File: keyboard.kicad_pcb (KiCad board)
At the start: 2 copper layers, 355 x 150.1 mm, 145 parts, among them SW1 SW_Push, SW10 SW_Push, SW11 SW_Push, SW12 SW_Push, SW13 SW_Push, SW14 SW_Push, SW15 SW_Push, SW16 SW_Push, SW17 SW_Push, SW18 SW_Push, SW19 SW_Push, SW2 SW_Push, SW20 SW_Push, SW21 SW_Push, SW22 SW_Push, SW23 SW_Push, SW24 SW_Push, SW25 SW_Push, SW26 SW_Push, SW27 SW_Push, SW28 SW_Push, SW29 SW_Push, SW3 SW_Push, SW30 SW_Push, SW31 SW_Push, SW32 SW_Push, SW33 SW_Push, SW34 SW_Push, SW35 SW_Push, SW36 SW_Push, SW37 SW_Push, SW38 SW_Push, SW39 SW_Push, SW4 SW_Push, SW40 SW_Push, SW41 SW_Push, SW42 SW_Push, SW43 SW_Push, SW44 SW_Push, SW45 SW_Push, SW46 SW_Push, SW47 SW_Push, SW48 SW_Push, SW49 SW_Push, SW5 SW_Push, SW50 SW_Push, SW51 SW_Push, SW52 SW_Push, SW53 SW_Push, SW54 SW_Push, SW55 SW_Push, SW56 SW_Push, SW57 SW_Push, SW58 SW_Push, SW59 SW_Push, SW6 SW_Push, SW60 SW_Push, SW61 SW_Push, SW62 SW_Push, SW63 SW_Push, SW64 SW_Push, SW7 SW_Push, SW8 SW_Push, SW9 SW_Push, U1 Pro Micro, U2 TRRS, U3 Pro Micro, U4 TRRS

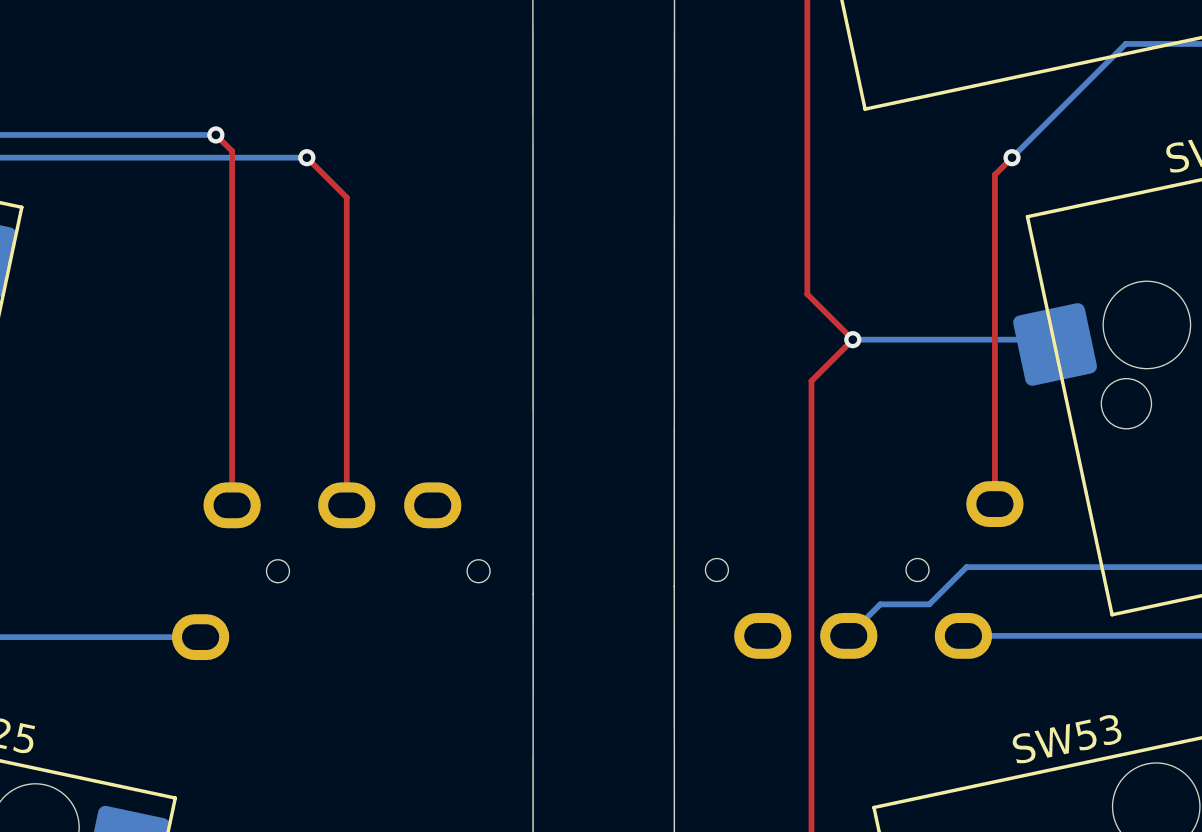
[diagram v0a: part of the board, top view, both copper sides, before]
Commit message: Move TRRS jacks around
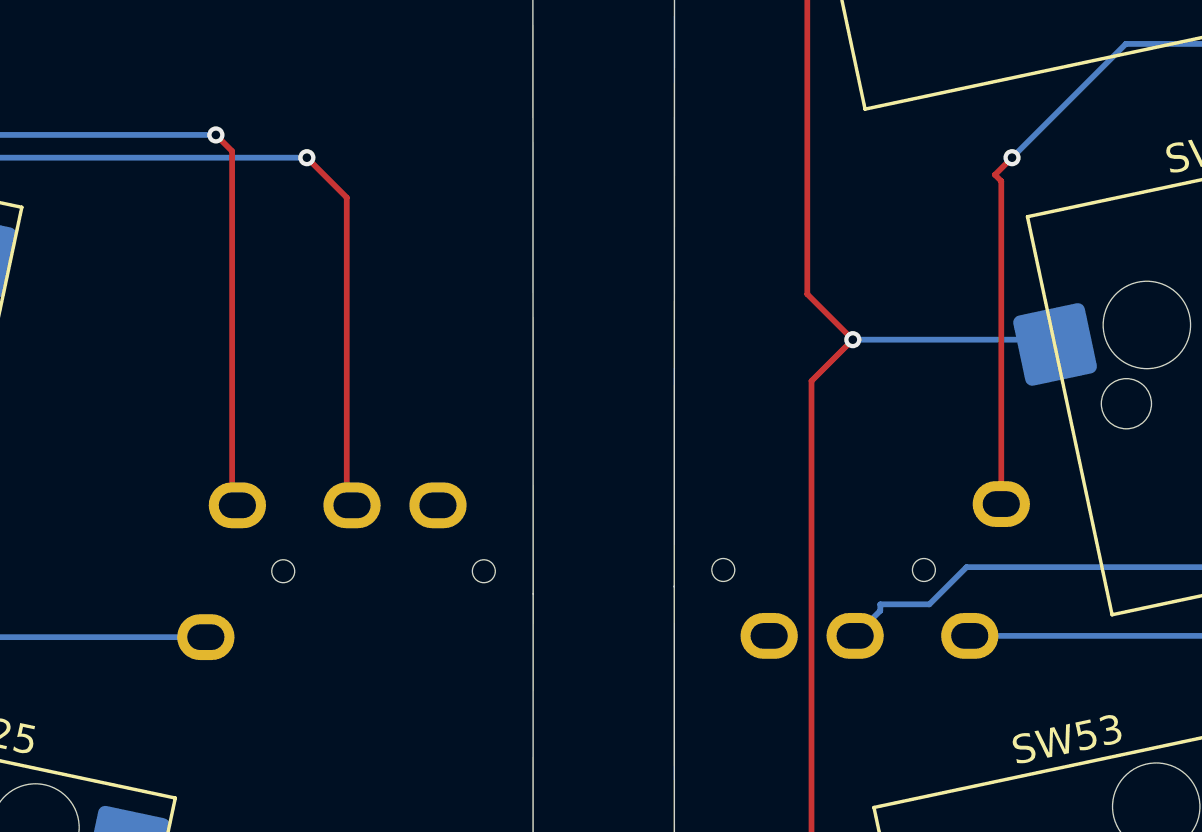
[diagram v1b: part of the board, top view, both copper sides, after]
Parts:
- moved U4 0.22 mm to (207.4, 152.5)
- moved U2 0.18 mm to (202.2, 152.5)
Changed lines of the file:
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@@
   )
   (footprint "Keebio-Parts:TRRS-PJ-320A" (layer "B.Cu")
-    (at 207.177606 152.499148 -90)
+    (at 207.4 152.499148 -90)
     (property "Sheetfile" "keyboard.kicad_sch")
     (property "Sheetname" "")
@@
   )
   (footprint "Keebio-Parts:TRRS-PJ-320A" (layer "B.Cu")
-    (at 202.060319 152.542852 90)
+    (at 202.243774 152.542852 90)
     (property "Sheetfile" "keyboard.kicad_sch")
     (property "Sheetname" "")
@@
   (segment (start 218.477606 138.709894) (end 219.075 138.1125) (width 0.2) (layer "F.Cu") (net 53))
   (segment (start 45.24375 89.877421) (end 46.790319 88.330852) (width 0.2) (layer "F.Cu") (net 53))
-  (segment (start 218.477606 150.199148) (end 218.477606 138.709894) (width 0.2) (layer "F.Cu") (net 53))
+  (segment (start 218.7 138.932288) (end 218.7 150.199148) (width 0.2) (layer "F.Cu") (net 53))
+  (segment (start 218.477606 138.709894) (end 218.7 138.932288) (width 0.2) (layer "F.Cu") (net 53))
   (via (at 375.44375 119.85625) (size 0.6) (drill 0.3) (layers "F.Cu" "B.Cu") (net 53))
   (via (at 219.075 138.1125) (size 0.6) (drill 0.3) (layers "F.Cu" "B.Cu") (net 53))
@@
   (segment (start 242.09375 149.225) (end 246.0625 145.25625) (width 0.2) (layer "B.Cu") (net 111))
   (segment (start 271.4625 141.2875) (end 286.54375 141.2875) (width 0.2) (layer "B.Cu") (net 111))
+  (segment (start 214.477606 153.699148) (end 214.477606 153.921542) (width 0.2) (layer "B.Cu") (net 111))
+  (segment (start 214.477606 153.921542) (end 213.6 154.799148) (width 0.2) (layer "B.Cu") (net 111))
   (segment (start 231.775 149.225) (end 242.09375 149.225) (width 0.2) (layer "B.Cu") (net 111))
-  (segment (start 213.377606 154.799148) (end 214.477606 153.699148) (width 0.2) (layer "B.Cu") (net 111))
   (segment (start 214.477606 153.699148) (end 216.188352 153.699148) (width 0.2) (layer "B.Cu") (net 111))
   (segment (start 384.216356 99.037112) (end 378.006638 99.037112) (width 0.2) (layer "B.Cu") (net 111))

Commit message: Clean up routes
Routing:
- net COL0: track 106.1 -> 102.4 mm
- net GND: track 419.4 -> 416.6 mm
- net ROW4: track 203.6 -> 202.3 mm
- net COL8: track 252.7 -> 253.6 mm

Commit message: Add ground fill
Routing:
- net GND: track 416.6 -> 4.66 mm, vias 4 -> 2
- added copper zone on B.Cu, net GND
- added copper zone on F.Cu, net GND
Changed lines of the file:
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@@
   (segment (start 165.1 131.7625) (end 161.13125 127.79375) (width 0.2) (layer "B.Cu") (net 51))
   (segment (start 44.701648 93.410852) (end 46.790319 93.410852) (width 0.2) (layer "B.Cu") (net 51))
-  (segment (start 219.075 138.557288) (end 219.075 138.1125) (width 0.2) (layer "F.Cu") (net 53))
-  (segment (start 375.44375 88.9) (end 375.44375 119.069994) (width 0.2) (layer "F.Cu") (net 53))
-  (segment (start 45.24375 89.877421) (end 45.24375 138) (width 0.2) (layer "F.Cu") (net 53))
-  (segment (start 218.7 138.932288) (end 219.075 138.557288) (width 0.2) (layer "F.Cu") (net 53))
-  (segment (start 46.790319 88.330852) (end 45.24375 89.877421) (width 0.2) (layer "F.Cu") (net 53))
-  (segment (start 218.7 150.199148) (end 218.7 138.932288) (width 0.2) (layer "F.Cu") (net 53))
-  (via (at 375.44375 119.069994) (size 0.6) (drill 0.3) (layers "F.Cu" "B.Cu") (net 53))
-  (via (at 219.075 138.1125) (size 0.6) (drill 0.3) (layers "F.Cu" "B.Cu") (net 53))
-  (via (at 45.24375 138) (size 0.6) (drill 0.3) (layers "F.Cu" "B.Cu") (net 53))
-  (via (at 375.44375 88.9) (size 0.6) (drill 0.3) (layers "F.Cu" "B.Cu") (net 53))
-  (segment (start 292.1 118.26875) (end 319.88125 118.26875) (width 0.2) (layer "B.Cu") (net 53))
-  (segment (start 375.436256 119.0625) (end 375.44375 119.069994) (width 0.2) (layer "B.Cu") (net 53))
-  (segment (start 127.375 142.875) (end 122.5 138) (width 0.2) (layer "B.Cu") (net 53))
-  (segment (start 320.675 119.0625) (end 375.436256 119.0625) (width 0.2) (layer "B.Cu") (net 53))
-  (segment (start 145 147) (end 140.875 142.875) (width 0.2) (layer "B.Cu") (net 53))
-  (segment (start 140.875 142.875) (end 127.375 142.875) (width 0.2) (layer "B.Cu") (net 53))
-  (segment (start 190.760319 154.842852) (end 186.917467 151) (width 0.2) (layer "B.Cu") (net 53))
-  (segment (start 375.44375 88.9) (end 375.420862 88.877112) (width 0.2) (layer "B.Cu") (net 53))
-  (segment (start 186.917467 151) (end 165.5 151) (width 0.2) (layer "B.Cu") (net 53))
-  (segment (start 375.420862 88.877112) (end 368.976356 88.877112) (width 0.2) (layer "B.Cu") (net 53))
-  (segment (start 161.5 147) (end 145 147) (width 0.2) (layer "B.Cu") (net 53))
-  (segment (start 165.5 151) (end 161.5 147) (width 0.2) (layer "B.Cu") (net 53))
-  (segment (start 122.5 138) (end 45.24375 138) (width 0.2) (layer "B.Cu") (net 53))
-  (segment (start 243.70625 127.79375) (end 257.175 127.79375) (width 0.2) (layer "B.Cu") (net 53))
-  (segment (start 290.5125 119.85625) (end 292.1 118.26875) (width 0.2) (layer "B.Cu") (net 53))
-  (segment (start 225.1875 132) (end 239.5 132) (width 0.2) (layer "B.Cu") (net 53))
-  (segment (start 219.075 138.1125) (end 225.1875 132) (width 0.2) (layer "B.Cu") (net 53))
-  (segment (start 273.84375 119.85625) (end 290.5125 119.85625) (width 0.2) (layer "B.Cu") (net 53))
-  (segment (start 257.175 127.79375) (end 260.35 124.61875) (width 0.2) (layer "B.Cu") (net 53))
-  (segment (start 319.88125 118.26875) (end 320.675 119.0625) (width 0.2) (layer "B.Cu") (net 53))
-  (segment (start 239.5 132) (end 243.70625 127.79375) (width 0.2) (layer "B.Cu") (net 53))
-  (segment (start 260.35 124.61875) (end 269.08125 124.61875) (width 0.2) (layer "B.Cu") (net 53))
-  (segment (start 269.08125 124.61875) (end 273.84375 119.85625) (width 0.2) (layer "B.Cu") (net 53))
+  (via (at 188.9125 153.9875) (size 0.6) (drill 0.3) (layers "F.Cu" "B.Cu") (net 53))
+  (via (at 217.4875 148.43125) (size 0.6) (drill 0.3) (layers "F.Cu" "B.Cu") (net 53))
+  (segment (start 218.7 150.199148) (end 218.7 149.64375) (width 0.2) (layer "B.Cu") (net 53))
+  (segment (start 189.767852 154.842852) (end 188.9125 153.9875) (width 0.2) (layer "B.Cu") (net 53))
+  (segment (start 190.943774 154.842852) (end 189.767852 154.842852) (width 0.2) (layer "B.Cu") (net 53))
+  (segment (start 218.7 149.64375) (end 217.4875 148.43125) (width 0.2) (layer "B.Cu") (net 53))
   (segment (start 249.599542 103.430851) (end 248.775811 104.254582) (width 0.2) (layer "B.Cu") (net 55))
   (segment (start 248.063699 97.239338) (end 249.599542 98.775181) (width 0.2) (layer "B.Cu") (net 55))
@@
   (segment (start 289.71875 138.1125) (end 377.825 138.1125) (width 0.2) (layer "B.Cu") (net 111))
   (segment (start 217.4875 152.4) (end 228.6 152.4) (width 0.2) (layer "B.Cu") (net 111))
+  (zone (net 53) (net_name "GND") (layers "F&B.Cu") (hatch edge 0.5)
+    (connect_pads (clearance 0.5))
+    (min_thickness 0.25) (filled_areas_thickness no)
+    (fill yes (thermal_gap 0.5) (thermal_bridge_width 0.5))
+    (polygon
+      (pts
+        (xy 34.13125 62.70625)
+        (xy 31.75 223.8375)
+        (xy 400.05 230.1875)
+        (xy 398.4625 56.35625)
+      )
+    )
+  )
 )
